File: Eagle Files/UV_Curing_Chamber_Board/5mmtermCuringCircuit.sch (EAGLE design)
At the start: 29 parts, among them IC1 7805T, IC2 L293D, T1 RFP30N06LE, T2 RFP30N06LE

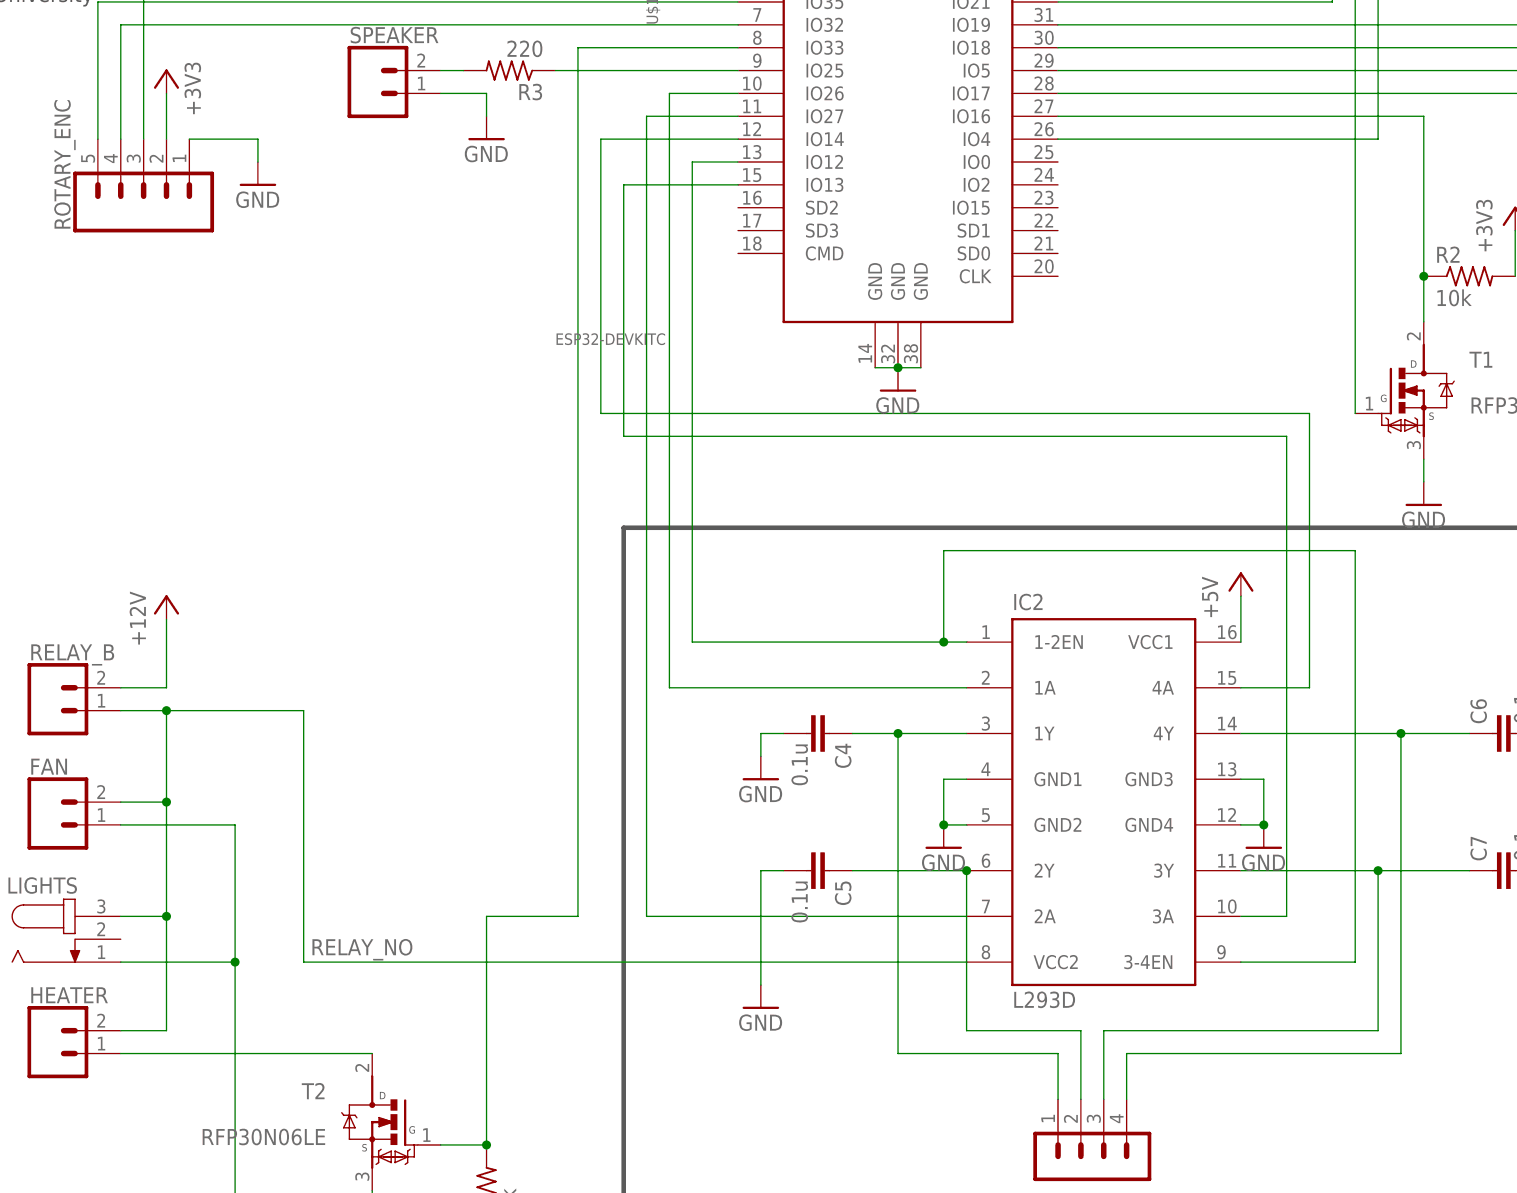
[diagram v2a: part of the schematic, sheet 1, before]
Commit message: Power changes to motor chip
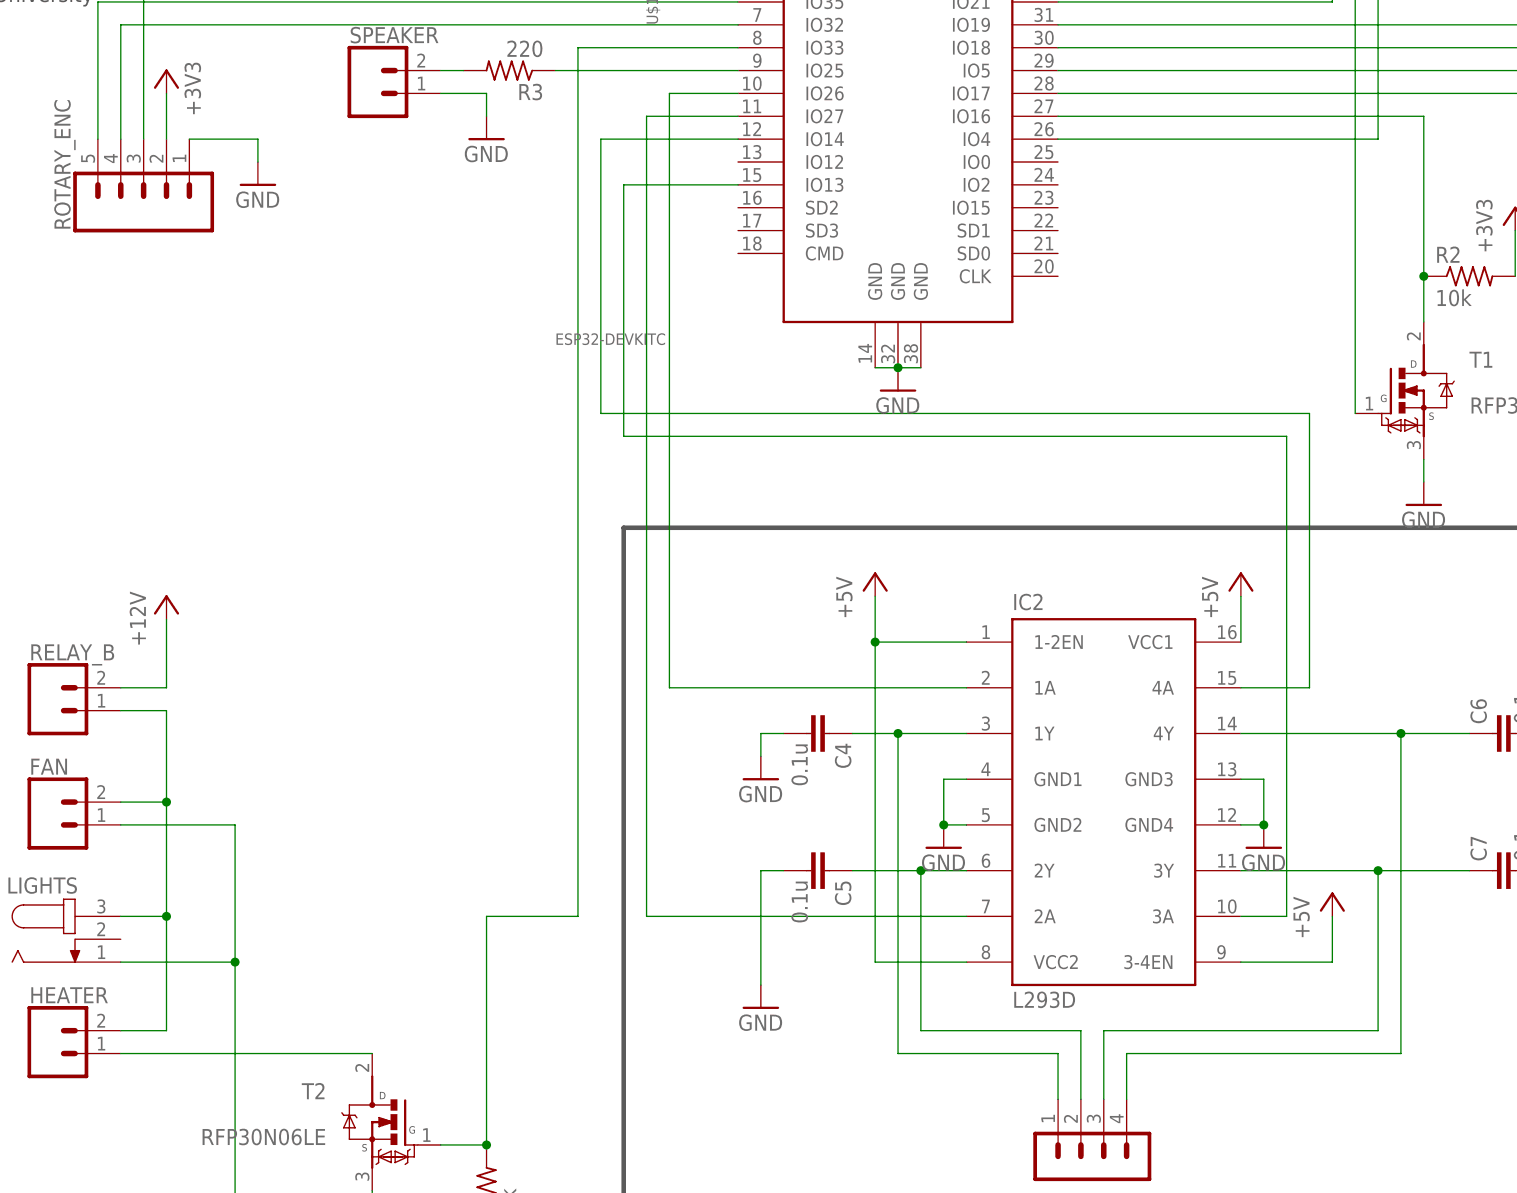
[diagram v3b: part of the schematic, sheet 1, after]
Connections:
- removed net N$12: IC2.1-2EN, IC2.3-4EN, U$1.IO12
- removed net RELAY_NO: FAN.2, HEATER.2, IC2.VCC2, LIGHTS.3, RELAY_B.1
- new net N$28: FAN.2, HEATER.2, LIGHTS.3, RELAY_B.1
- net +5V: now also IC2.1-2EN, IC2.3-4EN, IC2.VCC2
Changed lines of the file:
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@@
 <?xml version="1.0" encoding="utf-8"?>
 <!DOCTYPE eagle SYSTEM "eagle.dtd">
-<eagle version="9.4.0">
+<eagle version="9.4.1">
 <drawing>
 <settings>
@@
 <part name="P+2" library="supply1" library_urn="urn:adsk.eagle:library:371" deviceset="+5V" device=""/>
 <part name="FRAME1" library="frames" library_urn="urn:adsk.eagle:library:229" deviceset="FRAME_B_L" device=""/>
-<part name="P+7" library="supply1" library_urn="urn:adsk.eagle:library:371" deviceset="+5V" device=""/>
 <part name="P+8" library="supply1" library_urn="urn:adsk.eagle:library:371" deviceset="+5V" device=""/>
 <part name="GND15" library="supply1" library_urn="urn:adsk.eagle:library:371" deviceset="GND" device=""/>
@@
 <part name="12V" library="supply2" library_urn="urn:adsk.eagle:library:372" deviceset="V+" device="" value="+12V"/>
 <part name="12V1" library="supply2" library_urn="urn:adsk.eagle:library:372" deviceset="V+" device="" value="+12V"/>
+<part name="P+3" library="supply1" library_urn="urn:adsk.eagle:library:371" deviceset="+5V" device=""/>
+<part name="P+4" library="supply1" library_urn="urn:adsk.eagle:library:371" deviceset="+5V" device=""/>
+<part name="P+5" library="supply1" library_urn="urn:adsk.eagle:library:371" deviceset="+5V" device=""/>
 </parts>
 <sheets>
@@
 <attribute name="DRAWING_NAME" x="340.36" y="24.13" size="2.54" layer="94"/>
 </instance>
-<instance part="P+7" gate="1" x="279.4" y="121.92" smashed="yes">
-<attribute name="VALUE" x="276.86" y="116.84" size="1.778" layer="96" rot="R90"/>
-</instance>
 <instance part="P+8" gate="1" x="388.62" y="172.72" smashed="yes">
 <attribute name="VALUE" x="386.08" y="167.64" size="1.778" layer="96" rot="R90"/>
@@
 <instance part="12V1" gate="1" x="160.02" y="119.38" smashed="yes">
 <attribute name="VALUE" x="157.734" y="113.792" size="1.778" layer="96" rot="R90"/>
+</instance>
+<instance part="P+3" gate="1" x="238.76" y="121.92" smashed="yes">
+<attribute name="VALUE" x="236.22" y="116.84" size="1.778" layer="96" rot="R90"/>
+</instance>
+<instance part="P+4" gate="1" x="279.4" y="121.92" smashed="yes">
+<attribute name="VALUE" x="276.86" y="116.84" size="1.778" layer="96" rot="R90"/>
+</instance>
+<instance part="P+5" gate="1" x="289.56" y="86.36" smashed="yes">
+<attribute name="VALUE" x="287.02" y="81.28" size="1.778" layer="96" rot="R90"/>
 </instance>
 </instances>
@@
 </segment>
 </net>
-<net name="RELAY_NO" class="1">
-<segment>
-<wire x1="154.94" y1="106.68" x2="160.02" y2="106.68" width="0.1524" layer="91"/>
-<wire x1="175.26" y1="78.74" x2="175.26" y2="106.68" width="0.1524" layer="91"/>
-<wire x1="175.26" y1="106.68" x2="160.02" y2="106.68" width="0.1524" layer="91"/>
-<pinref part="HEATER" gate="G$1" pin="2"/>
-<pinref part="FAN" gate="G$1" pin="2"/>
-<wire x1="160.02" y1="96.52" x2="154.94" y2="96.52" width="0.1524" layer="91"/>
-<wire x1="160.02" y1="96.52" x2="160.02" y2="83.82" width="0.1524" layer="91"/>
-<pinref part="LIGHTS" gate="G$1" pin="3"/>
-<wire x1="154.94" y1="83.82" x2="160.02" y2="83.82" width="0.1524" layer="91"/>
-<junction x="160.02" y="83.82"/>
-<wire x1="160.02" y1="83.82" x2="160.02" y2="71.12" width="0.1524" layer="91"/>
-<wire x1="160.02" y1="71.12" x2="154.94" y2="71.12" width="0.1524" layer="91"/>
-<wire x1="160.02" y1="96.52" x2="160.02" y2="106.68" width="0.1524" layer="91"/>
-<junction x="160.02" y="96.52"/>
-<junction x="160.02" y="106.68"/>
-<label x="176.022" y="79.502" size="1.778" layer="95"/>
-<pinref part="RELAY_B" gate="G$1" pin="1"/>
-<pinref part="IC2" gate="G$1" pin="VCC2"/>
-<wire x1="175.26" y1="78.74" x2="248.92" y2="78.74" width="0.1524" layer="91"/>
-</segment>
-</net>
 <net name="N$6" class="0">
 <segment>
@@
 </segment>
 </net>
-<net name="N$12" class="0">
-<segment>
-<wire x1="248.92" y1="114.3" x2="246.38" y2="114.3" width="0.1524" layer="91"/>
-<wire x1="246.38" y1="114.3" x2="246.38" y2="124.46" width="0.1524" layer="91"/>
-<wire x1="246.38" y1="124.46" x2="292.1" y2="124.46" width="0.1524" layer="91"/>
-<wire x1="292.1" y1="124.46" x2="292.1" y2="78.74" width="0.1524" layer="91"/>
-<wire x1="292.1" y1="78.74" x2="279.4" y2="78.74" width="0.1524" layer="91"/>
-<pinref part="IC2" gate="G$1" pin="1-2EN"/>
-<pinref part="IC2" gate="G$1" pin="3-4EN"/>
-<pinref part="U$1" gate="G$1" pin="IO12"/>
-<wire x1="218.44" y1="167.64" x2="223.52" y2="167.64" width="0.1524" layer="91"/>
-<wire x1="218.44" y1="167.64" x2="218.44" y2="114.3" width="0.1524" layer="91"/>
-<wire x1="246.38" y1="114.3" x2="218.44" y2="114.3" width="0.1524" layer="91"/>
-<junction x="246.38" y="114.3"/>
-</segment>
-</net>
 <net name="N$2" class="0">
 <segment>
@@
 </segment>
 <segment>
-<pinref part="P+7" gate="1" pin="+5V"/>
-<wire x1="279.4" y1="119.38" x2="279.4" y2="114.3" width="0.1524" layer="91"/>
-<pinref part="IC2" gate="G$1" pin="VCC1"/>
-</segment>
-<segment>
 <wire x1="388.62" y1="170.18" x2="388.62" y2="165.1" width="0.1524" layer="91"/>
 <pinref part="R1" gate="G$1" pin="2"/>
@@
 <wire x1="236.22" y1="213.36" x2="236.22" y2="205.74" width="0.1524" layer="91"/>
 <junction x="236.22" y="205.74"/>
+</segment>
+<segment>
+<pinref part="P+3" gate="1" pin="+5V"/>
+<wire x1="238.76" y1="114.3" x2="238.76" y2="119.38" width="0.1524" layer="91"/>
+<pinref part="IC2" gate="G$1" pin="1-2EN"/>
+<wire x1="248.92" y1="114.3" x2="238.76" y2="114.3" width="0.1524" layer="91"/>
+<junction x="238.76" y="114.3"/>
+<pinref part="IC2" gate="G$1" pin="VCC2"/>
+<wire x1="248.92" y1="78.74" x2="238.76" y2="78.74" width="0.1524" layer="91"/>
+<wire x1="238.76" y1="78.74" x2="238.76" y2="114.3" width="0.1524" layer="91"/>
+</segment>
+<segment>
+<wire x1="279.4" y1="119.38" x2="279.4" y2="114.3" width="0.1524" layer="91"/>
+<pinref part="IC2" gate="G$1" pin="VCC1"/>
+<pinref part="P+4" gate="1" pin="+5V"/>
+</segment>
+<segment>
+<pinref part="IC2" gate="G$1" pin="3-4EN"/>
+<wire x1="279.4" y1="78.74" x2="289.56" y2="78.74" width="0.1524" layer="91"/>
+<pinref part="P+5" gate="1" pin="+5V"/>
+<wire x1="289.56" y1="78.74" x2="289.56" y2="83.82" width="0.1524" layer="91"/>
 </segment>
 </net>
@@
 <net name="N$7" class="0">
 <segment>
-<pinref part="IC2" gate="G$1" pin="2Y"/>
-<wire x1="248.92" y1="88.9" x2="248.92" y2="71.12" width="0.1524" layer="91"/>
-<wire x1="248.92" y1="71.12" x2="261.62" y2="71.12" width="0.1524" layer="91"/>
+<wire x1="243.84" y1="71.12" x2="261.62" y2="71.12" width="0.1524" layer="91"/>
 <pinref part="MOTOR_BREAKOUT" gate="1" pin="2"/>
 <wire x1="261.62" y1="71.12" x2="261.62" y2="63.5" width="0.1524" layer="91"/>
+<pinref part="IC2" gate="G$1" pin="2Y"/>
 <pinref part="C5" gate="G$1" pin="1"/>
-<wire x1="236.22" y1="88.9" x2="248.92" y2="88.9" width="0.1524" layer="91"/>
-<junction x="248.92" y="88.9"/>
+<wire x1="236.22" y1="88.9" x2="243.84" y2="88.9" width="0.1524" layer="91"/>
+<wire x1="243.84" y1="88.9" x2="248.92" y2="88.9" width="0.1524" layer="91"/>
+<wire x1="243.84" y1="71.12" x2="243.84" y2="88.9" width="0.1524" layer="91"/>
+<junction x="243.84" y="88.9"/>
 </segment>
 </net>
@@
 </segment>
 </net>
+<net name="N$28" class="1">
+<segment>
+<pinref part="RELAY_B" gate="G$1" pin="1"/>
+<wire x1="154.94" y1="106.68" x2="160.02" y2="106.68" width="0.1524" layer="91"/>
+<pinref part="HEATER" gate="G$1" pin="2"/>
+<wire x1="160.02" y1="71.12" x2="154.94" y2="71.12" width="0.1524" layer="91"/>
+<pinref part="LIGHTS" gate="G$1" pin="3"/>
+<wire x1="154.94" y1="83.82" x2="160.02" y2="83.82" width="0.1524" layer="91"/>
+<junction x="160.02" y="83.82"/>
+<wire x1="160.02" y1="83.82" x2="160.02" y2="71.12" width="0.1524" layer="91"/>
+<pinref part="FAN" gate="G$1" pin="2"/>
+<wire x1="160.02" y1="96.52" x2="154.94" y2="96.52" width="0.1524" layer="91"/>
+<wire x1="160.02" y1="96.52" x2="160.02" y2="83.82" width="0.1524" layer="91"/>
+<wire x1="160.02" y1="96.52" x2="160.02" y2="106.68" width="0.1524" layer="91"/>
+<junction x="160.02" y="96.52"/>
+</segment>
+</net>
